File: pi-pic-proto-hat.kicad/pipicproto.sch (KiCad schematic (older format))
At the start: 23 parts, among them J1 Conn_01x02_Male, J10 Conn_01x13_Male, J2 Conn_01x02_Male, J22 Conn_01x13_Male, J3 Conn_01x02_Male, J6 Barrel_Jack_Switch, J7 Conn_01x20_Male, J8 Conn_01x06_Male, J9 Conn_01x02_Male, P1 Conn_02x20_Odd_Even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

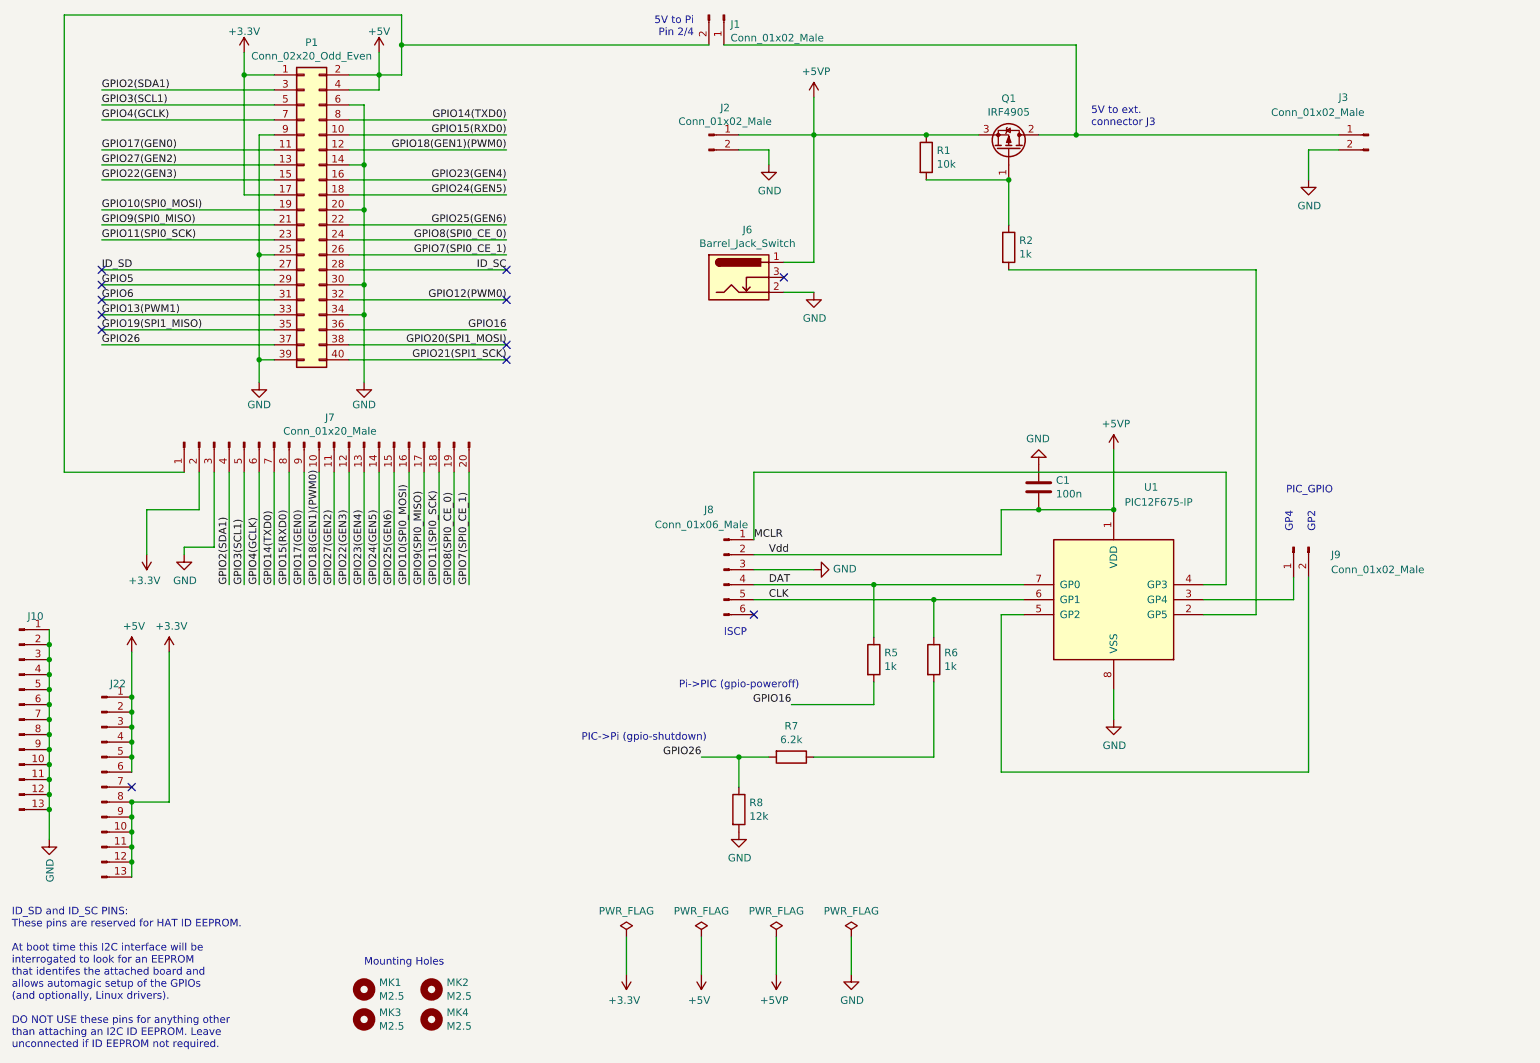
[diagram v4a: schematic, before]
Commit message: V2.04: place jumper J1 between J6 (barrel-jack) and ICSP-connector
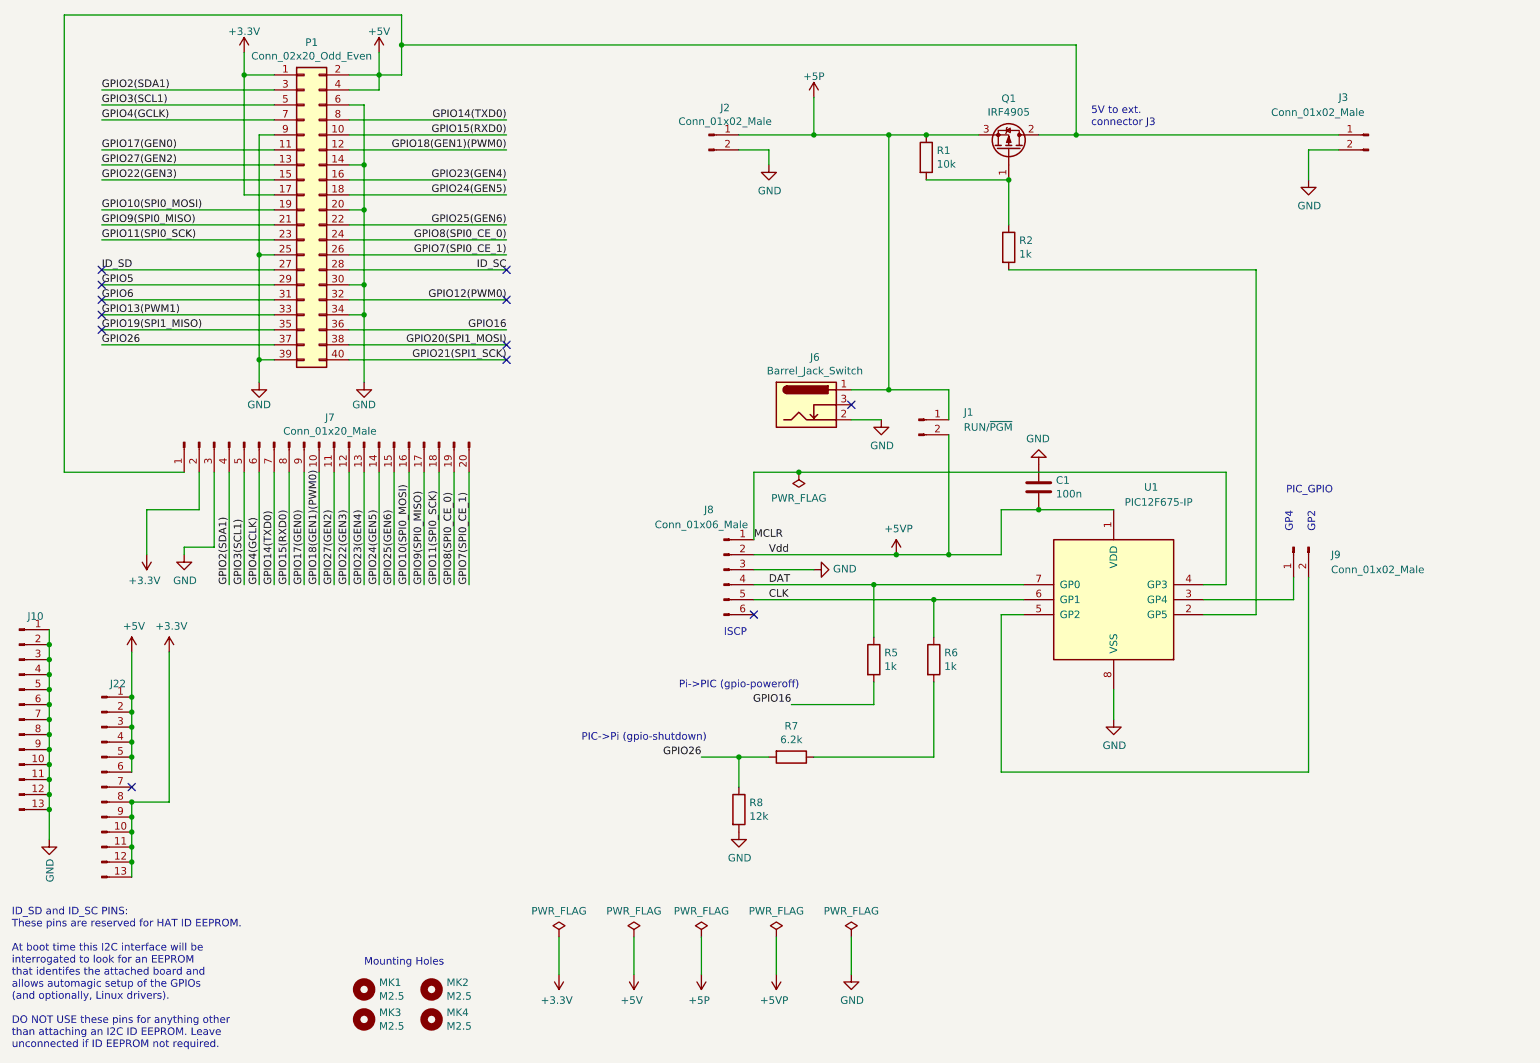
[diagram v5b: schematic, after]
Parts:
- J1: value Conn_01x02_Male -> RUN/~PGM~
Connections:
- net +5V: now also J3.1 (Pin_1), Q1.2 (D); no longer J1.2 (Pin_2)
- net +5VP: now also J1.2 (Pin_2); no longer J2.1 (Pin_1), J6.1, Q1.3 (S), R1.1
- new net +5P: J1.1 (Pin_1), J2.1 (Pin_1), J6.1, Q1.3 (S), R1.1
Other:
- note removed: "5V to Pi\nPin 2/4"
- moved on the sheet: J1, J6
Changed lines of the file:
@@
 Title "PI PIC Prototyping Area"
 Date "2020-06-22"
-Rev "2.03"
+Rev "2.04"
 Comp "Bernhard Bablok, Lothar Hiller"
 Comment1 "https://github.com/bablokb/pi-pic-proto-hat"
@@
 GPIO7(SPI0_CE_1)
 $Comp
-L power:+5VP #PWR03
-U 1 1 5E3C4C39
-P 6000 1250
-F 0 "#PWR03" H 6000 1100 50  0001 C CNN
-F 1 "+5VP" H 6015 1423 50  0000 C CNN
-F 2 "" H 6000 1250 50  0001 C CNN
-F 3 "" H 6000 1250 50  0001 C CNN
-	1    6000 1250
-	1    0    0    -1
-$EndComp
-$Comp
 L power:+5VP #PWR010
 U 1 1 5E3C6A1E
-P 8000 3600
-F 0 "#PWR010" H 8000 3450 50  0001 C CNN
-F 1 "+5VP" H 8015 3773 50  0000 C CNN
-F 2 "" H 8000 3600 50  0001 C CNN
-F 3 "" H 8000 3600 50  0001 C CNN
-	1    8000 3600
+P 6550 4300
+F 0 "#PWR010" H 6550 4150 50  0001 C CNN
+F 1 "+5VP" H 6565 4473 50  0000 C CNN
+F 2 "" H 6550 4300 50  0001 C CNN
+F 3 "" H 6550 4300 50  0001 C CNN
+	1    6550 4300
 	1    0    0    -1
 $EndComp
@@
 	5600 4400 6000 4400
 Wire Wire Line
-	5600 4300 7250 4300
+	5600 4300 6550 4300
 Wire Wire Line
 	7250 4300 7250 4000
@@
 Wire Wire Line
 	5600 3750 5600 4200
-Wire Wire Line
-	8750 3750 5600 3750
 Wire Wire Line
 	8600 4600 9200 4600
@@
 	7100 1500 6750 1500
 Wire Wire Line
-	6750 1500 6000 1500
+	6750 1500 6500 1500
 Connection ~ 6750 1500
 Wire Wire Line
@@
 Wire Wire Line
 	8000 5200 8000 5400
-Wire Wire Line
-	8000 4000 8000 3600
-Connection ~ 8000 4000
 $Comp
 L power:PWR_FLAG #FLG01
 U 1 1 5E605EFF
-P 4750 6850
-F 0 "#FLG01" H 4750 6925 50  0001 C CNN
-F 1 "PWR_FLAG" H 4750 7023 50  0000 C CNN
-F 2 "" H 4750 6850 50  0001 C CNN
-F 3 "~" H 4750 6850 50  0001 C CNN
-	1    4750 6850
+P 4300 6850
+F 0 "#FLG01" H 4300 6925 50  0001 C CNN
+F 1 "PWR_FLAG" H 4300 7023 50  0000 C CNN
+F 2 "" H 4300 6850 50  0001 C CNN
+F 3 "~" H 4300 6850 50  0001 C CNN
+	1    4300 6850
 	1    0    0    -1
 $EndComp
@@
 L power:+3.3V #PWR018
 U 1 1 5E6081FA
-P 4750 7100
-F 0 "#PWR018" H 4750 6950 50  0001 C CNN
-F 1 "+3.3V" H 4765 7273 50  0000 C CNN
-F 2 "" H 4750 7100 50  0001 C CNN
-F 3 "" H 4750 7100 50  0001 C CNN
-	1    4750 7100
+P 4300 7100
+F 0 "#PWR018" H 4300 6950 50  0001 C CNN
+F 1 "+3.3V" H 4315 7273 50  0000 C CNN
+F 2 "" H 4300 7100 50  0001 C CNN
+F 3 "" H 4300 7100 50  0001 C CNN
+	1    4300 7100
 	-1   0    0    1
 $EndComp
 $Comp
-L power:+5V #PWR019
+L power:+5P #PWR019
 U 1 1 5E617B7B
 P 5250 7100
 F 0 "#PWR019" H 5250 6950 50  0001 C CNN
-F 1 "+5V" H 5265 7273 50  0000 C CNN
+F 1 "+5P" H 5265 7273 50  0000 C CNN
 F 2 "" H 5250 7100 50  0001 C CNN
 F 3 "" H 5250 7100 50  0001 C CNN
@@
 	5250 6850 5250 7100
 Wire Wire Line
-	4750 6850 4750 7100
+	4300 6850 4300 7100
 $Comp
 L power:GND #PWR06
 U 1 1 5E422B40
-P 6000 2550
-F 0 "#PWR06" H 6000 2300 50  0001 C CNN
-F 1 "GND" H 6005 2377 50  0000 C CNN
-F 2 "" H 6000 2550 50  0001 C CNN
-F 3 "" H 6000 2550 50  0001 C CNN
-	1    6000 2550
-	1    0    0    -1
-$EndComp
-Wire Wire Line
-	6000 2550 5800 2550
-NoConn ~ 5800 2450
+P 6450 3400
+F 0 "#PWR06" H 6450 3150 50  0001 C CNN
+F 1 "GND" H 6455 3227 50  0000 C CNN
+F 2 "" H 6450 3400 50  0001 C CNN
+F 3 "" H 6450 3400 50  0001 C CNN
+	1    6450 3400
+	1    0    0    -1
+$EndComp
+Wire Wire Line
+	6450 3400 6250 3400
+NoConn ~ 6250 3300
 Wire Wire Line
 	5500 1500 6000 1500
@@
 Wire Wire Line
 	5700 1600 5700 1700
-Wire Wire Line
-	5800 2350 6000 2350
-Wire Wire Line
-	6000 2350 6000 1500
 $Comp
 L Connector:Barrel_Jack_Switch J6
 U 1 1 5E3F667C
-P 5500 2450
-F 0 "J6" H 5557 2767 50  0000 C CNN
-F 1 "Barrel_Jack_Switch" H 5557 2676 50  0000 C CNN
-F 2 "Connector_BarrelJack:BarrelJack_CUI_PJ-102AH_Horizontal" H 5550 2410 50  0001 C CNN
-F 3 "~" H 5550 2410 50  0001 C CNN
-	1    5500 2450
+P 5950 3300
+F 0 "J6" H 6007 3617 50  0000 C CNN
+F 1 "Barrel_Jack_Switch" H 6007 3526 50  0000 C CNN
+F 2 "Connector_BarrelJack:BarrelJack_CUI_PJ-102AH_Horizontal" H 6000 3260 50  0001 C CNN
+F 3 "~" H 6000 3260 50  0001 C CNN
+	1    5950 3300
 	1    0    0    -1
 $EndComp
@@
 L Connector:Conn_01x02_Male J1
 U 1 1 5E41F5B6
-P 5400 700
-F 0 "J1" V 5462 744 50  0000 L CNN
-F 1 "Conn_01x02_Male" V 5553 744 50  0000 L CNN
-F 2 "Connector_PinHeader_2.54mm:PinHeader_1x02_P2.54mm_Vertical" H 5400 700 50  0001 C CNN
-F 3 "~" H 5400 700 50  0001 C CNN
-	1    5400 700
-	0    1    1    0
-$EndComp
-Wire Wire Line
-	5300 900  3250 900
+P 6700 3400
+F 0 "J1" H 7000 3450 50  0000 L CNN
+F 1 "RUN/~PGM~" H 7000 3350 50  0000 L CNN
+F 2 "Connector_PinHeader_2.54mm:PinHeader_1x02_P2.54mm_Vertical" H 6700 3400 50  0001 C CNN
+F 3 "~" H 6700 3400 50  0001 C CNN
+	1    6700 3400
+	1    0    0    -1
+$EndComp
 Connection ~ 3250 900
 Wire Wire Line
@@
 Wire Wire Line
 	7500 1500 7750 1500
-Wire Wire Line
-	5400 900  7750 900
 Wire Wire Line
 	7750 900  7750 1500
@@
 	1700 5950 1450 5950
 Connection ~ 1450 5950
-Text Notes 5200 850  2    50   ~ 0
-5V to Pi\nPin 2/4
 Text Notes 7850 1450 0    50   ~ 0
 5V to ext.\nconnector J3 \n
@@
 Text Notes 9350 4150 1    50   ~ 0
 GP2
+Connection ~ 6900 4300
+Wire Wire Line
+	6900 4300 7250 4300
+Wire Wire Line
+	6900 3400 6900 3200
+Wire Wire Line
+	3250 900  7750 900
+Connection ~ 6550 4300
+Wire Wire Line
+	6550 4300 6900 4300
+Wire Wire Line
+	6250 3200 6500 3200
+Wire Wire Line
+	6500 3200 6500 1500
+Connection ~ 6500 3200
+Wire Wire Line
+	6500 3200 6900 3200
+Connection ~ 6500 1500
+Wire Wire Line
+	6500 1500 6000 1500
+Wire Wire Line
+	6900 3500 6900 4300
+Wire Wire Line
+	5600 3750 5900 3750
+$Comp
+L power:+5P #PWR0103
+U 1 1 5F0543B9
+P 6000 1250
+F 0 "#PWR0103" H 6000 1100 50  0001 C CNN
+F 1 "+5P" H 6000 1390 50  0000 C CNN
+F 2 "" H 6000 1250 50  0000 C CNN
+F 3 "" H 6000 1250 50  0000 C CNN
+	1    6000 1250
+	1    0    0    -1
+$EndComp
+$Comp
+L power:PWR_FLAG #FLG0101
+U 1 1 5F05503B
+P 5900 3750
+F 0 "#FLG0101" H 5900 3825 50  0001 C CNN
+F 1 "PWR_FLAG" H 5900 3923 50  0000 C CNN
+F 2 "" H 5900 3750 50  0001 C CNN
+F 3 "~" H 5900 3750 50  0001 C CNN
+	1    5900 3750
+	-1   0    0    1
+$EndComp
+Connection ~ 5900 3750
+Wire Wire Line
+	5900 3750 8750 3750
+$Comp
+L power:PWR_FLAG #FLG0102
+U 1 1 5F06C550
+P 4800 6850
+F 0 "#FLG0102" H 4800 6925 50  0001 C CNN
+F 1 "PWR_FLAG" H 4800 7023 50  0000 C CNN
+F 2 "" H 4800 6850 50  0001 C CNN
+F 3 "~" H 4800 6850 50  0001 C CNN
+	1    4800 6850
+	1    0    0    -1
+$EndComp
+$Comp
+L power:+5V #PWR0104
+U 1 1 5F06C55A
+P 4800 7100
+F 0 "#PWR0104" H 4800 6950 50  0001 C CNN
+F 1 "+5V" H 4815 7273 50  0000 C CNN
+F 2 "" H 4800 7100 50  0001 C CNN
+F 3 "" H 4800 7100 50  0001 C CNN
+	1    4800 7100
+	-1   0    0    1
+$EndComp
+Wire Wire Line
+	4800 6850 4800 7100
 $EndSCHEMATC

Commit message: V2.06: remove R6 (not needed, since we added a voltage-divider)
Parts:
- removed R6: 1k, Resistor_THT:R_Axial_DIN0207_L6.3mm_D2.5mm_P10.16mm_Horizontal, symbol Device:R
- J7: value Conn_01x20_Male -> Conn_01x24_Male; footprint Connector_PinHeader_2.54mm:PinHeader_1x20_P2.54mm_Vertical -> Connector_PinHeader_2.54mm:PinHeader_1x24_P2.54mm_Vertical; symbol Connector:Conn_01x20_Male -> Connector:Conn_01x24_Male
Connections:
- net +3V3: no longer J7.2 (Pin_2)
- net +5V: no longer J7.1 (Pin_1)
- net CLK: now also R7.1
- net GND: no longer J7.3 (Pin_3)
- net GPIO10(SPI0_MOSI): now also J7.13 (Pin_13); no longer J7.16 (Pin_16)
- net GPIO11(SPI0_SCK): now also J7.15 (Pin_15); no longer J7.18 (Pin_18)
- net GPIO12(PWM0): now also J7.20 (Pin_20)
- net GPIO13(PWM1): now also J7.21 (Pin_21)
- net GPIO14(TXD0): now also J7.4 (Pin_4); no longer J7.7 (Pin_7)
- net GPIO15(RXD0): now also J7.5 (Pin_5); no longer J7.8 (Pin_8)
- net GPIO17(GEN0): now also J7.6 (Pin_6); no longer J7.9 (Pin_9)
- net GPIO18(GEN1)(PWM0): now also J7.7 (Pin_7); no longer J7.10 (Pin_10)
- net GPIO19(SPI1_MISO): now also J7.22 (Pin_22)
- net GPIO2(SDA1): now also J7.1 (Pin_1); no longer J7.4 (Pin_4)
- net GPIO20(SPI1_MOSI): now also J7.23 (Pin_23)
- net GPIO21(SPI1_SCK): now also J7.24 (Pin_24)
- net GPIO22(GEN3): now also J7.9 (Pin_9); no longer J7.12 (Pin_12)
- net GPIO23(GEN4): now also J7.10 (Pin_10); no longer J7.13 (Pin_13)
- net GPIO24(GEN5): now also J7.11 (Pin_11); no longer J7.14 (Pin_14)
- net GPIO25(GEN6): now also J7.12 (Pin_12); no longer J7.15 (Pin_15)
- net GPIO27(GEN2): now also J7.8 (Pin_8); no longer J7.11 (Pin_11)
- net GPIO3(SCL1): now also J7.2 (Pin_2); no longer J7.5 (Pin_5)
- net GPIO4(GCLK): now also J7.3 (Pin_3); no longer J7.6 (Pin_6)
- net GPIO5: now also J7.18 (Pin_18)
- net GPIO6: now also J7.19 (Pin_19)
- net GPIO7(SPI0_CE_1): now also J7.17 (Pin_17); no longer J7.20 (Pin_20)
- net GPIO8(SPI0_CE_0): now also J7.16 (Pin_16); no longer J7.19 (Pin_19)
- net GPIO9(SPI0_MISO): now also J7.14 (Pin_14); no longer J7.17 (Pin_17)
- no-connect marks 12 -> 5
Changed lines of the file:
@@
 Sheet 1 1
 Title "PI PIC Prototyping Area"
-Date "2020-06-22"
-Rev "2.04"
+Date "2020-06-29"
+Rev "2.06"
 Comp "Bernhard Bablok, Lothar Hiller"
 Comment1 "https://github.com/bablokb/pi-pic-proto-hat"
@@
 $EndComp
 $Comp
-L Device:R R6
-U 1 1 5E3133D0
-P 6800 5000
-F 0 "R6" H 6870 5046 50  0000 L CNN
-F 1 "1k" H 6870 4955 50  0000 L CNN
-F 2 "Resistor_THT:R_Axial_DIN0207_L6.3mm_D2.5mm_P10.16mm_Horizontal" V 6730 5000 50  0001 C CNN
-F 3 "~" H 6800 5000 50  0001 C CNN
-	1    6800 5000
-	1    0    0    -1
-$EndComp
-$Comp
 L Device:R R5
 U 1 1 5E312AD7
@@
 $EndComp
 $Comp
-L Connector:Conn_01x20_Male J7
+L Connector:Conn_01x24_Male J7
 U 1 1 5E364D51
 P 2700 3550
 F 0 "J7" V 2535 3478 50  0000 C CNN
-F 1 "Conn_01x20_Male" V 2626 3478 50  0000 C CNN
-F 2 "Connector_PinHeader_2.54mm:PinHeader_1x20_P2.54mm_Vertical" H 2700 3550 50  0001 C CNN
+F 1 "Conn_01x24_Male" V 2626 3478 50  0000 C CNN
+F 2 "Connector_PinHeader_2.54mm:PinHeader_1x24_P2.54mm_Vertical" H 2700 3550 50  0001 C CNN
 F 3 "~" H 2700 3550 50  0001 C CNN
 	1    2700 3550
@@
 $EndComp
 Wire Wire Line
+	1600 3750 1600 4500
+Wire Wire Line
+	1700 3750 1700 4500
+Wire Wire Line
+	3250 1100 3100 1100
+Text Label 1600 4500 1    50   ~ 0
+GPIO2(SDA1)
+Text Label 1700 4500 1    50   ~ 0
+GPIO3(SCL1)
+Wire Wire Line
+	1800 3750 1800 4500
+Wire Wire Line
+	1900 3750 1900 4500
+Wire Wire Line
+	2000 3750 2000 4500
+Wire Wire Line
 	2100 3750 2100 4500
 Wire Wire Line
 	2200 3750 2200 4500
-$Comp
-L power:+3.3V #PWR012
-U 1 1 5E3732E4
-P 1550 4300
-F 0 "#PWR012" H 1550 4150 50  0001 C CNN
-F 1 "+3.3V" H 1565 4473 50  0000 C CNN
-F 2 "" H 1550 4300 50  0001 C CNN
-F 3 "" H 1550 4300 50  0001 C CNN
-	1    1550 4300
-	-1   0    0    1
-$EndComp
-$Comp
-L power:GND #PWR013
-U 1 1 5E375515
-P 1800 4300
-F 0 "#PWR013" H 1800 4050 50  0001 C CNN
-F 1 "GND" H 1805 4127 50  0000 C CNN
-F 2 "" H 1800 4300 50  0001 C CNN
-F 3 "" H 1800 4300 50  0001 C CNN
-	1    1800 4300
-	1    0    0    -1
-$EndComp
-Wire Wire Line
-	2000 3750 2000 4250
-Wire Wire Line
-	2000 4250 1800 4250
-Wire Wire Line
-	1800 4250 1800 4300
-Wire Wire Line
-	1900 3750 1900 4000
-Wire Wire Line
-	1900 4000 1550 4000
-Wire Wire Line
-	1550 4000 1550 4300
-Wire Wire Line
-	1800 3750 1000 3750
-Wire Wire Line
-	1000 3750 1000 700
-Wire Wire Line
-	1000 700  3250 700
-Wire Wire Line
-	3250 700  3250 900
-Wire Wire Line
-	3250 1100 3100 1100
+Wire Wire Line
+	2300 3750 2300 4500
+Wire Wire Line
+	2400 3750 2400 4500
+Wire Wire Line
+	2500 3750 2500 4500
+Wire Wire Line
+	2600 3750 2600 4500
+Wire Wire Line
+	2700 3750 2700 4500
+Wire Wire Line
+	2800 3750 2800 4500
+Wire Wire Line
+	2900 3750 2900 4500
+Wire Wire Line
+	3000 3750 3000 4500
+Wire Wire Line
+	3100 3750 3100 4500
+Wire Wire Line
+	3200 3750 3200 4500
+Text Label 1800 4500 1    50   ~ 0
+GPIO4(GCLK)
+Text Label 1900 4500 1    50   ~ 0
+GPIO14(TXD0)
+Text Label 2000 4500 1    50   ~ 0
+GPIO15(RXD0)
 Text Label 2100 4500 1    50   ~ 0
-GPIO2(SDA1)
+GPIO17(GEN0)
 Text Label 2200 4500 1    50   ~ 0
-GPIO3(SCL1)
-Wire Wire Line
-	2300 3750 2300 4500
-Wire Wire Line
-	2400 3750 2400 4500
-Wire Wire Line
-	2500 3750 2500 4500
-Wire Wire Line
-	2600 3750 2600 4500
-Wire Wire Line
-	2700 3750 2700 4500
-Wire Wire Line
-	2800 3750 2800 4500
-Wire Wire Line
-	2900 3750 2900 4500
-Wire Wire Line
-	3000 3750 3000 4500
-Wire Wire Line
-	3100 3750 3100 4500
-Wire Wire Line
-	3200 3750 3200 4500
-Wire Wire Line
-	3300 3750 3300 4500
-Wire Wire Line
-	3400 3750 3400 4500
-Wire Wire Line
-	3500 3750 3500 4500
-Wire Wire Line
-	3600 3750 3600 4500
-Wire Wire Line
-	3700 3750 3700 4500
+GPIO18(GEN1)(PWM0)
 Text Label 2300 4500 1    50   ~ 0
-GPIO4(GCLK)
+GPIO27(GEN2)
 Text Label 2400 4500 1    50   ~ 0
-GPIO14(TXD0)
+GPIO22(GEN3)
 Text Label 2500 4500 1    50   ~ 0
-GPIO15(RXD0)
+GPIO23(GEN4)
 Text Label 2600 4500 1    50   ~ 0
-GPIO17(GEN0)
+GPIO24(GEN5)
 Text Label 2700 4500 1    50   ~ 0
-GPIO18(GEN1)(PWM0)
+GPIO25(GEN6)
 Text Label 2800 4500 1    50   ~ 0
-GPIO27(GEN2)
+GPIO10(SPI0_MOSI)
 Text Label 2900 4500 1    50   ~ 0
-GPIO22(GEN3)
+GPIO9(SPI0_MISO)
 Text Label 3000 4500 1    50   ~ 0
-GPIO23(GEN4)
+GPIO11(SPI0_SCK)
 Text Label 3100 4500 1    50   ~ 0
-GPIO24(GEN5)
+GPIO8(SPI0_CE_0)
 Text Label 3200 4500 1    50   ~ 0
-GPIO25(GEN6)
-Text Label 3300 4500 1    50   ~ 0
-GPIO10(SPI0_MOSI)
-Text Label 3400 4500 1    50   ~ 0
-GPIO9(SPI0_MISO)
-Text Label 3500 4500 1    50   ~ 0
-GPIO11(SPI0_SCK)
-Text Label 3600 4500 1    50   ~ 0
-GPIO8(SPI0_CE_0)
-Text Label 3700 4500 1    50   ~ 0
 GPIO7(SPI0_CE_1)
 $Comp
@@
 	6400 4850 6400 4500
 Connection ~ 6400 4500
-Wire Wire Line
-	6800 4850 6800 4600
 Connection ~ 6800 4600
 Wire Wire Line
@@
 	9300 1600 9300 1800
 NoConn ~ 3950 2400
-NoConn ~ 3950 2600
-NoConn ~ 3950 2900
-NoConn ~ 3950 3000
 NoConn ~ 1250 2400
-NoConn ~ 1250 2500
-NoConn ~ 1250 2600
-NoConn ~ 1250 2700
-NoConn ~ 1250 2800
 Wire Wire Line
 	900  4800 900  4900
@@
 	1    0    0    -1
 $EndComp
-Connection ~ 3250 900
 Wire Wire Line
 	3250 900  3250 1100
@@
 	6800 4600 7400 4600
 Wire Wire Line
-	6800 5150 6800 5650
-Wire Wire Line
 	6800 5650 6000 5650
 Wire Wire Line
@@
 Wire Wire Line
 	4800 6850 4800 7100
+Text Label 3700 3750 3    50   ~ 0
+GPIO19(SPI1_MISO)
+Text Label 3300 3750 3    50   ~ 0
+GPIO5
+Text Label 3400 3750 3    50   ~ 0
+GPIO6
+Text Label 3500 3750 3    50   ~ 0
+GPIO12(PWM0)
+Text Label 3600 3750 3    50   ~ 0
+GPIO13(PWM1)
+Text Label 3800 3750 3    50   ~ 0
+GPIO20(SPI1_MOSI)
+Text Label 3900 3750 3    50   ~ 0
+GPIO21(SPI1_SCK)
+Wire Wire Line
+	6800 4600 6800 5650
 $EndSCHEMATC
